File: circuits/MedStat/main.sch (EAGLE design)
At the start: 37 parts, among them U1 BLE113-VISUAL-A, U2 MMA8452Q

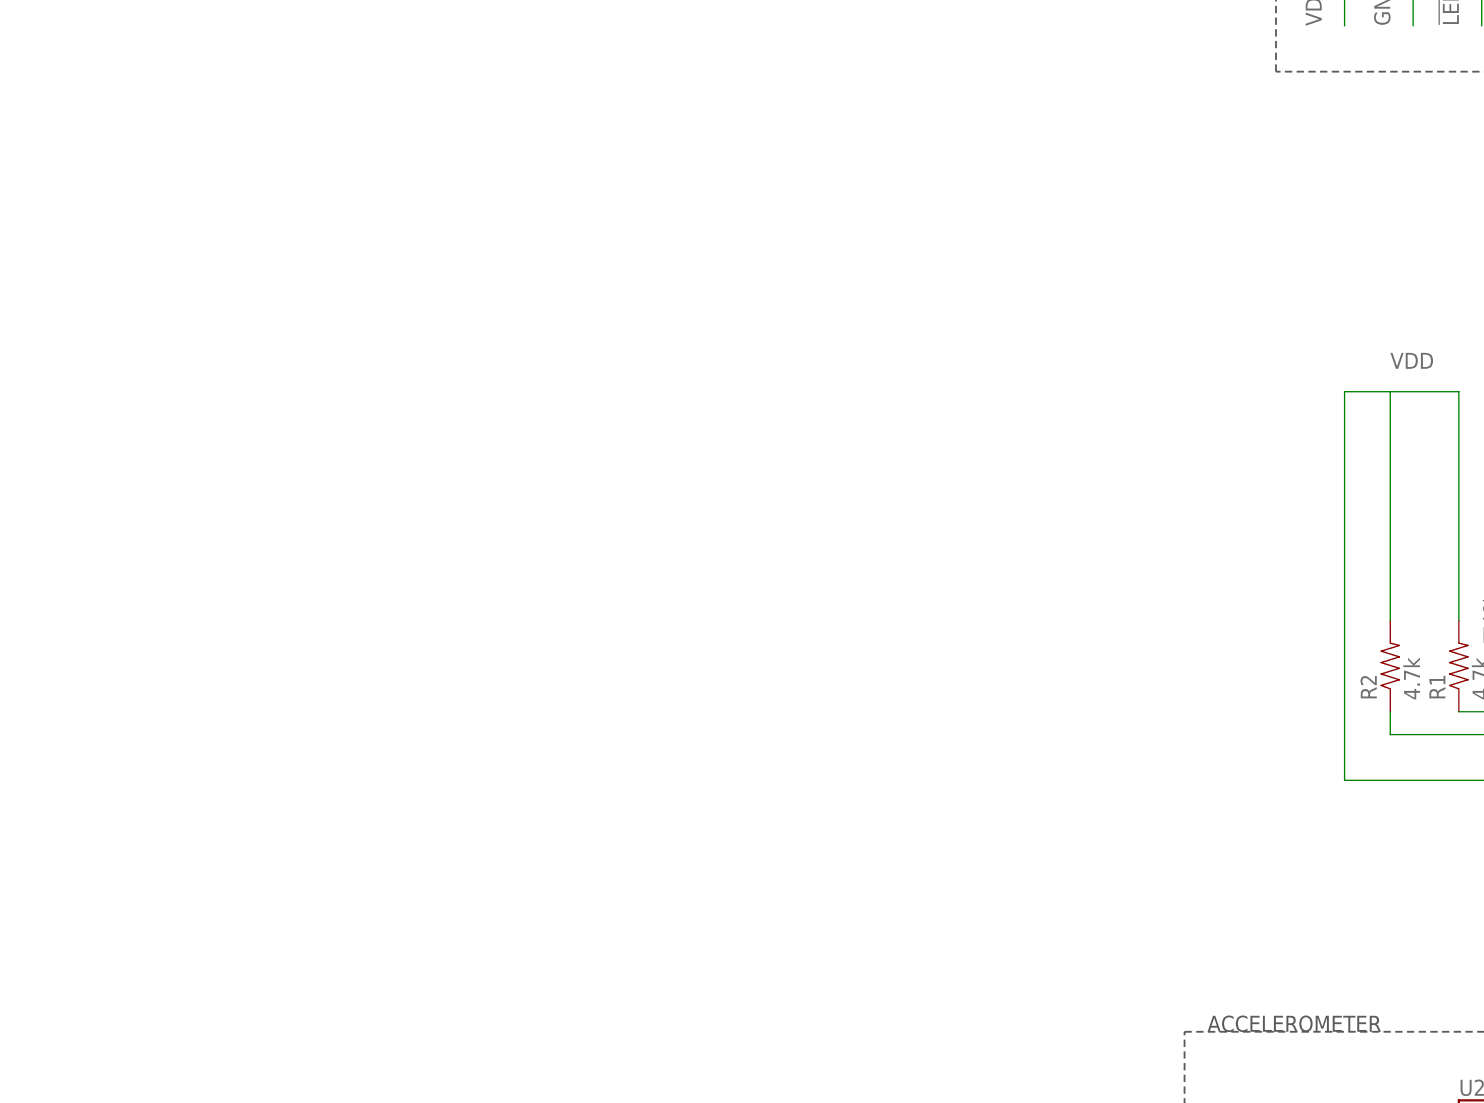
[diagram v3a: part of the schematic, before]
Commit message: added power circuit to main schematic
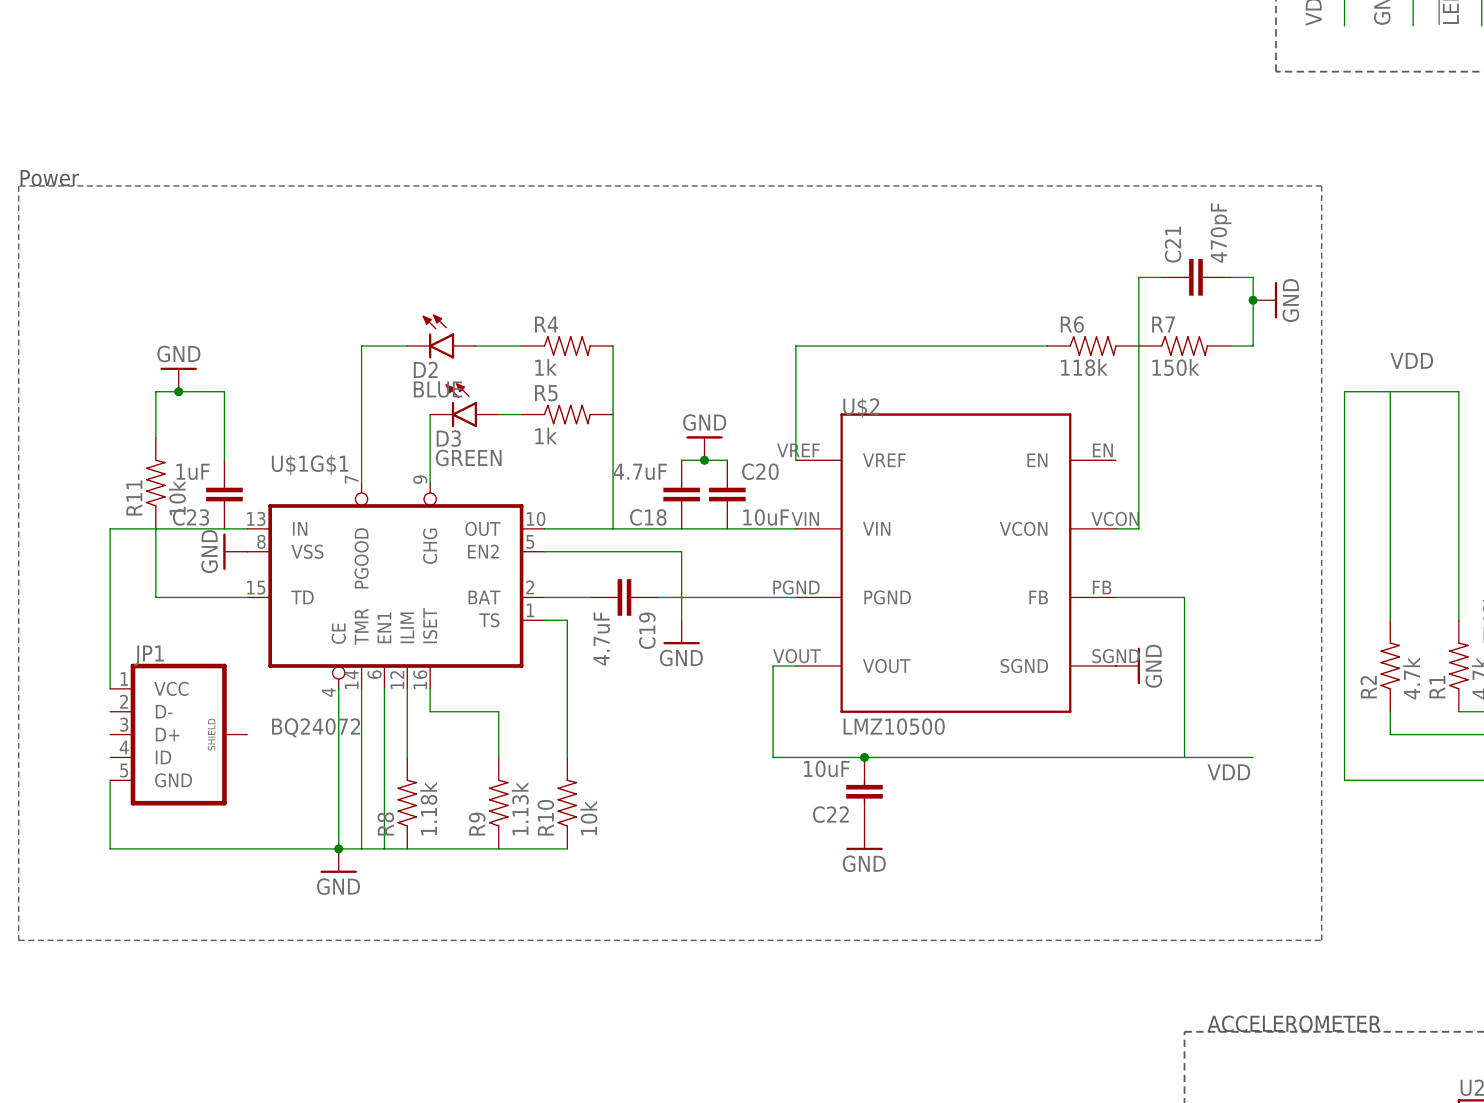
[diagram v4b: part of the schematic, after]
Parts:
- added C18, C19: 4.7uF, SparkFun-Passives:CAP0603-CAP
- added C20, C22: 10uF, SparkFun-Passives:CAP0603-CAP
- added C21: 470pF, SparkFun-Passives:CAP0603-CAP
- added C23: 1uF, SparkFun-Passives:CAP0603-CAP
- added D2: BLUE, SparkFun-LED:LED-BLUE0603
- added D3: GREEN, SparkFun-LED:LED-GREEN0603
- added JP1: (no value), SparkFun-Connectors:USB_MICROB_PLUG-SMT
- added R10, R11: 10k, SparkFun-Passives:RESISTOR0603-RES
- added R4, R5: 1k, SparkFun-Passives:RESISTOR0603-RES
- added R6: 118k, SparkFun-Passives:RESISTOR0603-RES
- added R7: 150k, SparkFun-Passives:RESISTOR0603-RES
- added R8: 1.18k, SparkFun-Passives:RESISTOR0603-RES
- added R9: 1.13k, SparkFun-Passives:RESISTOR0603-RES
- added U$1: BQ24072, Simplex-ICs:BQ24072
- added U$2: LMZ10500, LMZ10500:LMZ10500
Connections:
- new net N$48: C23.1, JP1.VCC, R11.1, U$1G$1.IN, U$1G$1.TD
- new net N$50: D3.A, R5.1
- new net N$51: D3.C, U$1G$1.CHG
- new net N$52: D2.C, U$1G$1.PGOOD
- new net N$53: D2.A, R4.1
- new net N$54: R8.2, U$1G$1.ILIM
- new net N$55: R9.2, U$1G$1.ISET
- new net N$56: R10.2, U$1G$1.TS
- new net N$58: R6.1, U$2.VREF
- new net N$59: C18.1, C20.2, R4.2, R5.2, U$1G$1.OUT, U$2.VIN
- new net N$60: C19.2, U$1G$1.BAT
- new net N$62: C21.1, R6.2, R7.1, U$2.VCON
- net GND: now also C18.2, C19.1, C20.1, C21.2, C22.1, C23.2, JP1.GND, R10.1, R11.2, R7.2, R8.1, R9.1, U$1G$1.CE, U$1G$1.EN1, U$1G$1.EN2, U$1G$1.TMR, U$1G$1.VSS, U$2.PGND, U$2.SGND
- net VDD: now also C22.2, U$2.FB, U$2.VOUT
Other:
- note added: "Power"

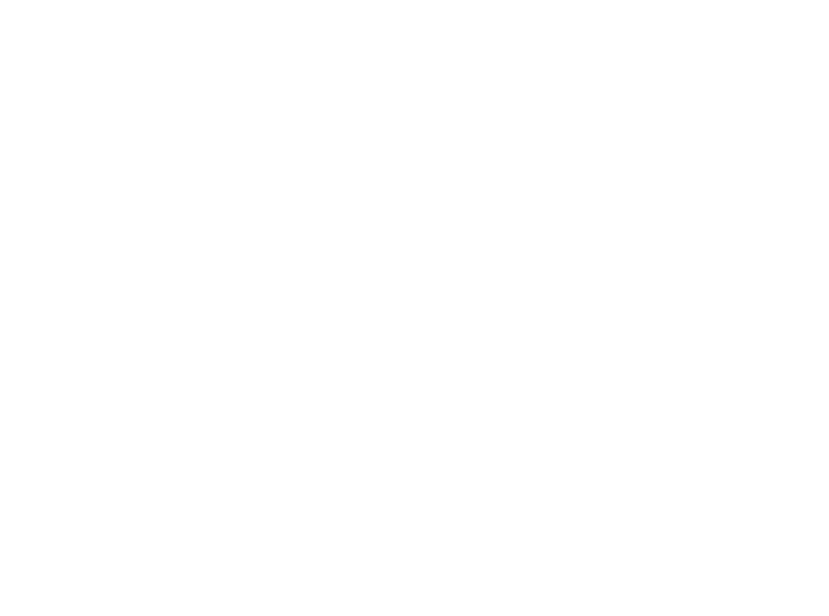
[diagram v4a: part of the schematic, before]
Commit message: Integrate into main schematic
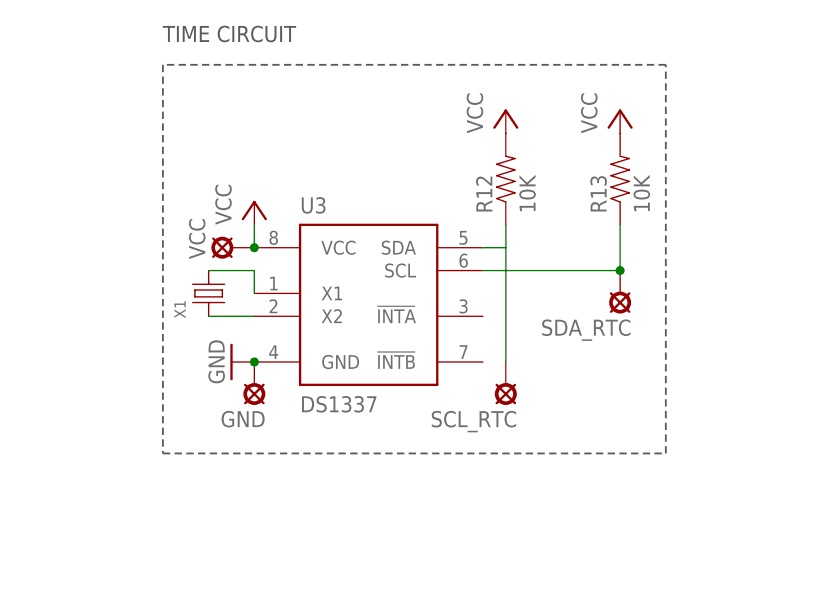
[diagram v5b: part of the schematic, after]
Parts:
- added GND, SCL_RTC, SDA_RTC, VCC: SE13, solpad:SE13
- added R12, R13: 10K, SparkFun-Resistors:10KOHM-1/10W-1%(0603)0603
- added U3: DS1337, ds1337:DS1337
- added X1: (no value), ds1337:CRYSTAL8X3.5MM
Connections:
- new net N$49: U3.X2, X1.1
- new net N$57: U3.X1, X1.3
- new net N$61: R12.1, SCL_RTC.MP, U3.SDA
- new net N$63: R13.1, SDA_RTC.MP, U3.SCL
- new net VCC: R12.2, R13.2, U3.VCC, VCC.MP
- net GND: now also GND.MP, U3.GND
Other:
- note added: "TIME CIRCUIT"
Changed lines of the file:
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@@
 <part name="JP1" library="SparkFun-Connectors" deviceset="USB_MICROB_PLUG" device="-SMT"/>
 <part name="GND26" library="SparkFun-Aesthetics" deviceset="GND" device=""/>
+<part name="X1" library="ds1337" deviceset="CRYSTAL" device="8X3.5MM"/>
+<part name="U3" library="ds1337" deviceset="DS1337" device=""/>
+<part name="P+1" library="supply1" deviceset="VCC" device=""/>
+<part name="P+2" library="supply1" deviceset="VCC" device=""/>
+<part name="P+3" library="supply1" deviceset="VCC" device=""/>
+<part name="R12" library="SparkFun-Resistors" deviceset="10KOHM-1/10W-1%(0603)" device="0603" value="10K"/>
+<part name="R13" library="SparkFun-Resistors" deviceset="10KOHM-1/10W-1%(0603)" device="0603" value="10K"/>
+<part name="GND27" library="supply1" deviceset="GND" device=""/>
+<part name="VCC" library="solpad" deviceset="SE13" device=""/>
+<part name="GND" library="solpad" deviceset="SE13" device=""/>
+<part name="SCL_RTC" library="solpad" deviceset="SE13" device=""/>
+<part name="SDA_RTC" library="solpad" deviceset="SE13" device=""/>
 </parts>
 <sheets>
@@
 <wire x1="-58.42" y1="50.8" x2="-203.2" y2="50.8" width="0.1524" layer="97" style="shortdash"/>
 <text x="-203.2" y="50.8" size="1.778" layer="97">Power</text>
+<wire x1="162.56" y1="101.6" x2="106.68" y2="101.6" width="0.2032" layer="97" style="shortdash"/>
+<wire x1="106.68" y1="101.6" x2="106.68" y2="58.42" width="0.2032" layer="97" style="shortdash"/>
+<wire x1="162.56" y1="58.42" x2="162.56" y2="101.6" width="0.2032" layer="97" style="shortdash"/>
+<wire x1="106.68" y1="58.42" x2="162.56" y2="58.42" width="0.2032" layer="97" style="shortdash"/>
+<text x="106.68" y="104.14" size="1.778" layer="97">TIME CIRCUIT</text>
 </plain>
 <instances>
@@
 <instance part="JP1" gate="G$1" x="-185.42" y="-10.16"/>
 <instance part="GND26" gate="1" x="-167.64" y="-25.4"/>
+<instance part="X1" gate="G$1" x="111.76" y="76.2" rot="R90"/>
+<instance part="U3" gate="G$1" x="121.92" y="83.82"/>
+<instance part="P+1" gate="VCC" x="116.84" y="86.36"/>
+<instance part="P+2" gate="VCC" x="144.78" y="96.52"/>
+<instance part="P+3" gate="VCC" x="157.48" y="96.52"/>
+<instance part="R12" gate="G$1" x="144.78" y="88.9" rot="R90"/>
+<instance part="R13" gate="G$1" x="157.48" y="88.9" rot="R90"/>
+<instance part="GND27" gate="1" x="114.3" y="68.58" rot="R270"/>
+<instance part="VCC" gate="1" x="114.3" y="81.28" rot="R90"/>
+<instance part="GND" gate="1" x="116.84" y="66.04" rot="R180"/>
+<instance part="SCL_RTC" gate="1" x="144.78" y="66.04" rot="R180"/>
+<instance part="SDA_RTC" gate="1" x="157.48" y="76.2" rot="R180"/>
 </instances>
 <busses>
@@
 <junction x="-167.64" y="-22.86"/>
 </segment>
+<segment>
+<pinref part="U3" gate="G$1" pin="GND"/>
+<pinref part="GND27" gate="1" pin="GND"/>
+<pinref part="GND" gate="1" pin="MP"/>
+<junction x="116.84" y="68.58"/>
+<pinref part="GND" gate="1" pin="MP"/>
+</segment>
 </net>
 <net name="SDA" class="0">
@@
 </segment>
 </net>
+<net name="N$49" class="0">
+<segment>
+<pinref part="X1" gate="G$1" pin="1"/>
+<pinref part="U3" gate="G$1" pin="X2"/>
+<wire x1="111.76" y1="73.66" x2="116.84" y2="73.66" width="0.1524" layer="91"/>
+</segment>
+</net>
+<net name="N$57" class="0">
+<segment>
+<pinref part="U3" gate="G$1" pin="X1"/>
+<wire x1="116.84" y1="76.2" x2="116.84" y2="78.74" width="0.1524" layer="91"/>
+<pinref part="X1" gate="G$1" pin="3"/>
+<wire x1="116.84" y1="78.74" x2="111.76" y2="78.74" width="0.1524" layer="91"/>
+</segment>
+</net>
+<net name="VCC" class="0">
+<segment>
+<pinref part="U3" gate="G$1" pin="VCC"/>
+<pinref part="P+1" gate="VCC" pin="VCC"/>
+<wire x1="116.84" y1="83.82" x2="116.84" y2="81.28" width="0.1524" layer="91"/>
+<pinref part="VCC" gate="1" pin="MP"/>
+<junction x="116.84" y="81.28"/>
+</segment>
+<segment>
+<pinref part="P+2" gate="VCC" pin="VCC"/>
+<pinref part="R12" gate="G$1" pin="2"/>
+</segment>
+<segment>
+<pinref part="P+3" gate="VCC" pin="VCC"/>
+<pinref part="R13" gate="G$1" pin="2"/>
+</segment>
+</net>
+<net name="N$61" class="0">
+<segment>
+<pinref part="R12" gate="G$1" pin="1"/>
+<wire x1="144.78" y1="68.58" x2="144.78" y2="81.28" width="0.1524" layer="91"/>
+<pinref part="SCL_RTC" gate="1" pin="MP"/>
+<pinref part="U3" gate="G$1" pin="SDA"/>
+<wire x1="144.78" y1="81.28" x2="144.78" y2="83.82" width="0.1524" layer="91"/>
+<wire x1="142.24" y1="81.28" x2="144.78" y2="81.28" width="0.1524" layer="91"/>
+</segment>
+</net>
+<net name="N$63" class="0">
+<segment>
+<pinref part="U3" gate="G$1" pin="SCL"/>
+<wire x1="142.24" y1="78.74" x2="157.48" y2="78.74" width="0.1524" layer="91"/>
+<pinref part="R13" gate="G$1" pin="1"/>
+<wire x1="157.48" y1="78.74" x2="157.48" y2="83.82" width="0.1524" layer="91"/>
+<pinref part="SDA_RTC" gate="1" pin="MP"/>
+<junction x="157.48" y="78.74"/>
+</segment>
+</net>
